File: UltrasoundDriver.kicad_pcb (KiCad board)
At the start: 2 copper layers, 113.8 x 41.1 mm, 52 parts, among them J1 Conn_01x05_Female, J2 Conn_01x05_Female, Q1 S8050, Q2 S8550, U1 MC33079, U2 L7815, U3 L7915, U4 MC33079

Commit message: first board iteration, JLC not done yet. Lotsa DRC errors tho
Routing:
- net Net-(LS1-Pad1): track 34.0 -> 29.0 mm
- net Net-(R16-Pad2): track 50.1 -> 48.7 mm
- net sigIn: track 70.6 -> 69.5 mm
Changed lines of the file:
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@@
   )
   (setup
+    (stackup
+      (layer "F.SilkS" (type "Top Silk Screen"))
+      (layer "F.Paste" (type "Top Solder Paste"))
+      (layer "F.Mask" (type "Top Solder Mask") (thickness 0.01))
+      (layer "F.Cu" (type "copper") (thickness 0.035))
+      (layer "dielectric 1" (type "core") (thickness 1.51) (material "FR4") (epsilon_r 4.5) (loss_tangent 0.02))
+      (layer "B.Cu" (type "copper") (thickness 0.035))
+      (layer "B.Mask" (type "Bottom Solder Mask") (thickness 0.01))
+      (layer "B.Paste" (type "Bottom Solder Paste"))
+      (layer "B.SilkS" (type "Bottom Silk Screen"))
+      (copper_finish "None")
+      (dielectric_constraints no)
+    )
     (pad_to_mask_clearance 0)
     (pcbplotparams
@@
   (segment (start 117.1956 39.9288) (end 124.535923 39.9288) (width 0.25) (layer "B.Cu") (net 1))
   (segment (start 99.0092 40.4368) (end 99.0092 39.9288) (width 0.25) (layer "B.Cu") (net 1))
-  (segment (start 100.2792 39.9288) (end 117.1956 39.9288) (width 0.25) (layer "B.Cu") (net 1))
   (segment (start 98.044 41.402) (end 99.0092 40.4368) (width 0.25) (layer "B.Cu") (net 1))
   (segment (start 69.083 48.26) (end 74.447 53.624) (width 0.25) (layer "B.Cu") (net 1))
   (segment (start 131.831 48.509) (end 103.886 76.454) (width 0.25) (layer "B.Cu") (net 1))
   (segment (start 48.26 48.26) (end 48.26 43.688) (width 0.25) (layer "B.Cu") (net 1))
-  (segment (start 99.0092 39.9288) (end 100.2792 39.9288) (width 0.25) (layer "B.Cu") (net 1))
+  (segment (start 99.0092 39.9288) (end 117.1956 39.9288) (width 0.25) (layer "B.Cu") (net 1))
   (segment (start 74.447 53.624) (end 88.1422 39.9288) (width 0.25) (layer "B.Cu") (net 1))
   (segment (start 94.488 71.244) (end 94.488 73.1898) (width 0.25) (layer "F.Cu") (net 2))
@@
   (segment (start 97.028 44.196) (end 97.028 46.039) (width 0.25) (layer "F.Cu") (net 17))
   (segment (start 97.282 43.18) (end 97.282 43.942) (width 0.25) (layer "F.Cu") (net 17))
-  (segment (start 73.655 57.912) (end 74.447 58.704) (width 0.25) (layer "F.Cu") (net 17))
   (segment (start 97.282 43.942) (end 97.028 44.196) (width 0.25) (layer "F.Cu") (net 17))
   (via (at 97.282 43.18) (size 0.8) (drill 0.4) (layers "F.Cu" "B.Cu") (net 17))
@@
   (segment (start 97.536 38.862) (end 98.298 39.624) (width 0.25) (layer "F.Cu") (net 20))
   (segment (start 80.4164 42.2148) (end 82.487 42.2148) (width 0.25) (layer "F.Cu") (net 20))
-  (segment (start 98.298 46.039) (end 98.298 46.486462) (width 0.25) (layer "F.Cu") (net 20))
   (segment (start 82.487 42.2148) (end 85.8398 38.862) (width 0.25) (layer "F.Cu") (net 20))
   (segment (start 93.218 46.99) (end 93.218 46.039) (width 0.25) (layer "F.Cu") (net 21))
@@
   (segment (start 88.664538 72.81) (end 91.624538 69.85) (width 0.25) (layer "F.Cu") (net 22))
   (segment (start 92.71 69.85) (end 93.218 70.358) (width 0.25) (layer "F.Cu") (net 22))
-  (segment (start 100.3672 58.9652) (end 99.314 57.912) (width 0.25) (layer "F.Cu") (net 23))
+  (segment (start 98.544 57.142) (end 100.3672 58.9652) (width 0.25) (layer "F.Cu") (net 23))
   (segment (start 105.2068 58.1152) (end 104.3568 58.9652) (width 0.25) (layer "F.Cu") (net 23))
-  (segment (start 98.544 57.142) (end 99.441 58.039) (width 0.25) (layer "F.Cu") (net 23))
   (segment (start 98.544 52.824) (end 98.544 57.142) (width 0.25) (layer "F.Cu") (net 23))
   (segment (start 104.3568 58.9652) (end 100.3672 58.9652) (width 0.25) (layer "F.Cu") (net 23))
@@
   (segment (start 103.5568 54.1142) (end 103.569 54.102) (width 0.25) (layer "F.Cu") (net 24))
   (segment (start 99.568 50.989) (end 100.456 50.989) (width 0.25) (layer "F.Cu") (net 24))
-  (segment (start 103.5568 58.0908) (end 103.5568 58.1152) (width 0.25) (layer "F.Cu") (net 24))
-  (segment (start 103.886 54.419) (end 103.569 54.102) (width 0.25) (layer "F.Cu") (net 24))
   (segment (start 100.456 50.989) (end 103.569 54.102) (width 0.25) (layer "F.Cu") (net 24))
   (segment (start 90.936462 48.26) (end 71.374 48.26) (width 0.25) (layer "F.Cu") (net 25))
@@
   (segment (start 88.6318 54.3052) (end 91.948 50.989) (width 0.25) (layer "F.Cu") (net 26))
   (segment (start 64.657 39.681) (end 62.407 39.681) (width 0.25) (layer "F.Cu") (net 26))
-  (segment (start 91.948 50.989) (end 91.948 50.541538) (width 0.25) (layer "F.Cu") (net 26))
   (segment (start 61.468 50.353206) (end 64.039795 52.925001) (width 0.25) (layer "F.Cu") (net 26))
   (segment (start 73.331 52.399) (end 82.2308 52.399) (width 0.25) (layer "F.Cu") (net 26))
-  (segment (start 65.004 39.878) (end 65.707 40.581) (width 0.25) (layer "F.Cu") (net 26))
   (segment (start 65.707 40.581) (end 65.557 40.581) (width 0.25) (layer "F.Cu") (net 26))
   (segment (start 62.407 39.681) (end 61.468 40.62) (width 0.25) (layer "F.Cu") (net 26))
@@
   (segment (start 124.142 42.7096) (end 125.5136 42.7096) (width 0.25) (layer "F.Cu") (net 28))
   (segment (start 124.142 40.0812) (end 124.142 42.7096) (width 0.25) (layer "F.Cu") (net 28))
-  (segment (start 130.556 47.752) (end 127.03 44.226) (width 0.25) (layer "B.Cu") (net 28))
   (zone (net 2) (net_name "GND") (layers F&B.Cu) (hatch edge 0.508)
     (connect_pads (clearance 0.508))

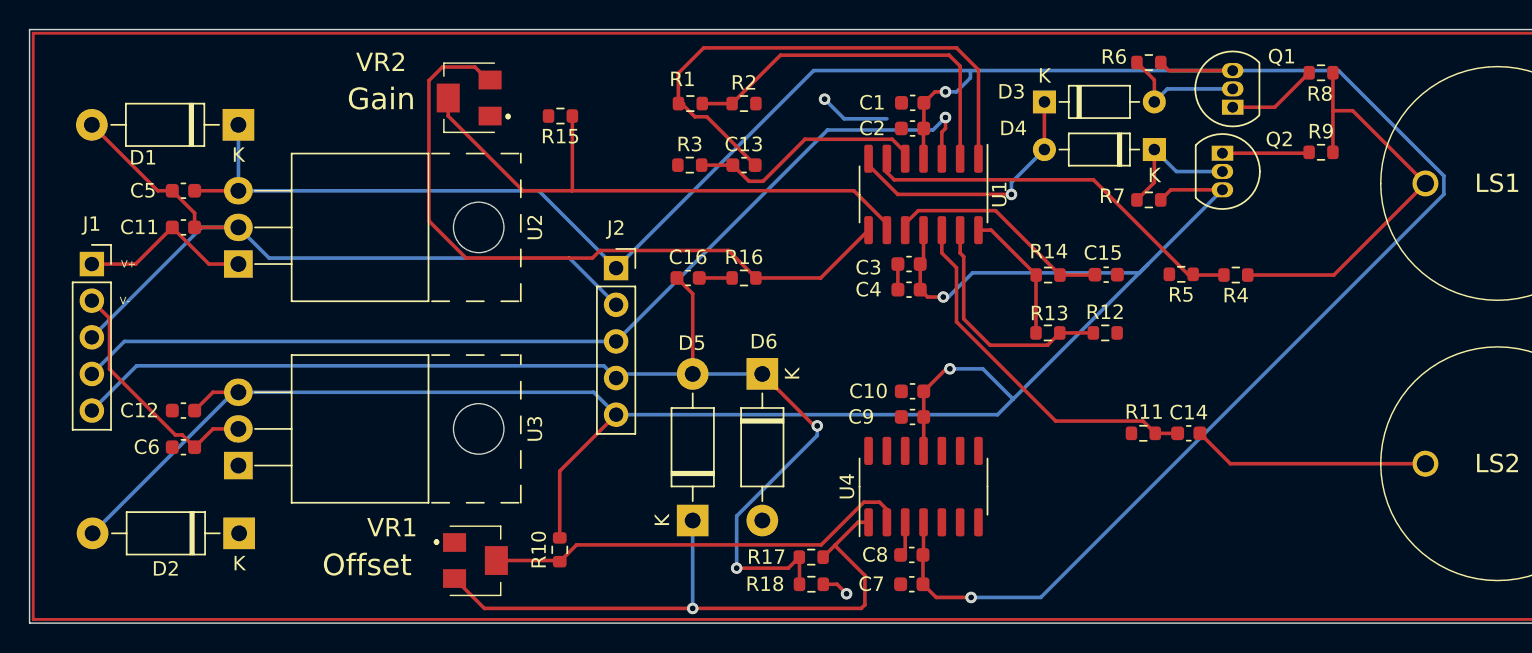
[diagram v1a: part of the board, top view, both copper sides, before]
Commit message: yeah I think this one is better, also updated resistor values after lab work
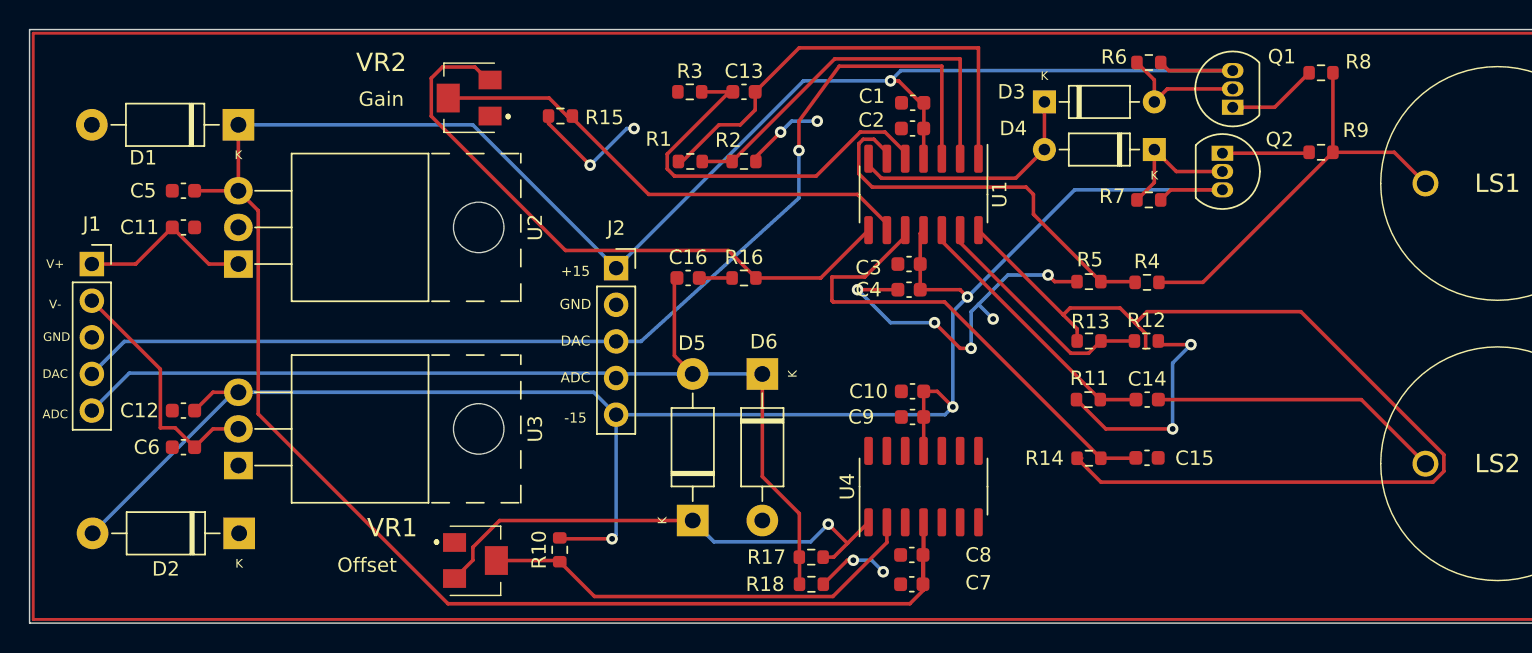
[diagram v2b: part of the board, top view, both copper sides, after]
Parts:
- R15: value 10k -> 100
- R4: value 4.7k -> 5.8k
- moved R14 13.0 mm to (107.2, 66.8)
- moved C15 13.0 mm to (111.3, 66.8)
- moved R5 6.42 mm to (107.2, 54.6)
- moved R4 6.18 mm to (111.3, 54.6)
- moved C13 5.08 mm to (83.3, 41.4)
- moved R3 5.08 mm to (79.6, 41.4)
- moved R11 4.47 mm to (107.2, 62.7)
- moved R1 4.01 mm to (79.6, 46.2)
- moved R2 4.01 mm to (83.3, 46.2)
- moved C14 3.71 mm to (111.3, 62.7)
- moved R12 2.91 mm to (111.2, 58.7)
- moved R13 2.91 mm to (107.2, 58.7)
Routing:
- net Net-(R13-Pad2): track 9.31 -> 71.9 mm
- net Net-(C15-Pad2): track 15.8 -> 33.9 mm
- net -15V: track 140.7 -> 128.2 mm, vias 2 -> 3
- net Net-(C13-Pad1): track 16.6 -> 28.5 mm
- net 3.3V: track 44.6 -> 35.3 mm
- net sigOut: track 79.4 -> 70.7 mm, vias 2 -> 0
- net sigIn: track 69.5 -> 77.4 mm
- net Net-(C14-Pad1): track 25.3 -> 18.8 mm
- net +15V: track 169.3 -> 175.4 mm, vias 2 -> 1
- net Net-(R15-Pad1): track 40.4 -> 34.5 mm
- net GND: track 66.5 -> 60.6 mm, vias 2 -> 13
- net Net-(C13-Pad2): track 37.9 -> 32.5 mm
- net Net-(R16-Pad2): track 48.7 -> 43.7 mm
- net Net-(C14-Pad2): track 16.5 -> 20.4 mm
- net Net-(R1-Pad2): track 26.0 -> 27.8 mm
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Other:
- board text added: "+15"
- board text added: "-15"
- board text added: "ADC"
- board text added: "DAC"
- board text added: "GND"

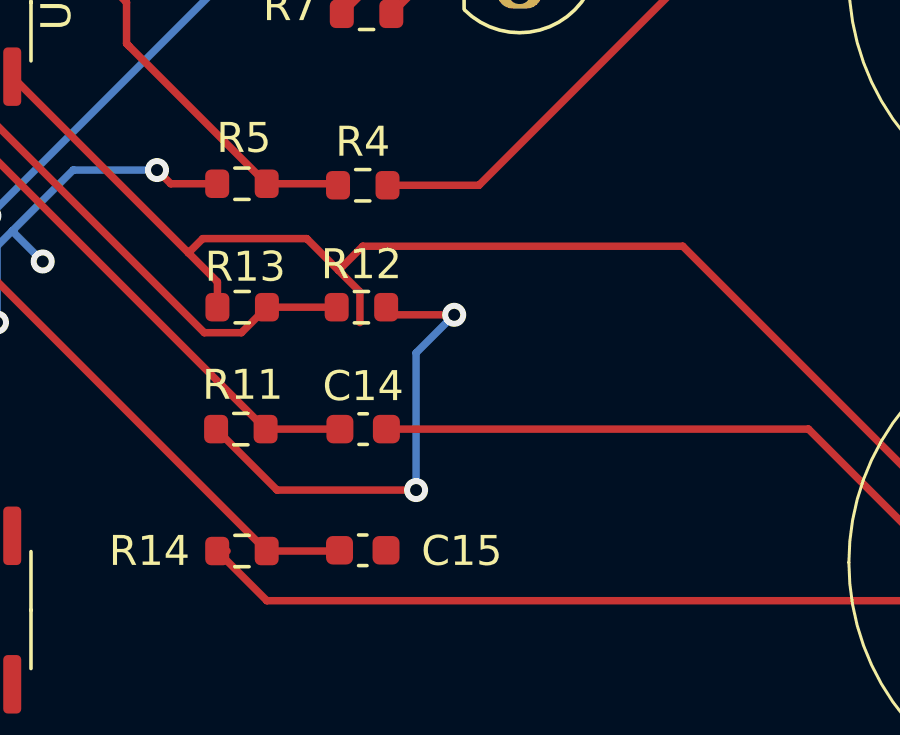
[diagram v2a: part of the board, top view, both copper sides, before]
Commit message: need to change footprint for tantalum caps
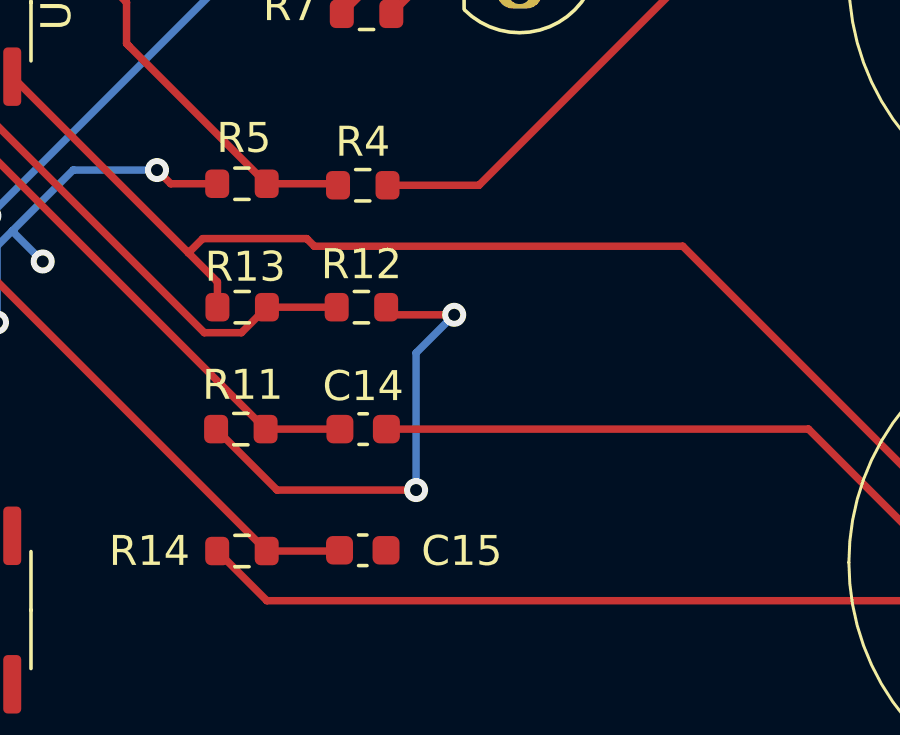
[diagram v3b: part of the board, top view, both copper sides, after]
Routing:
- net Net-(R13-Pad2): track 71.9 -> 68.9 mm
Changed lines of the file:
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@@
   (segment (start 103.4532 49.9628) (end 108.0496 54.5592) (width 0.25) (layer "F.Cu") (net 21))
   (segment (start 108.0496 54.5592) (end 110.3762 54.5592) (width 0.25) (layer "F.Cu") (net 21))
-  (segment (start 108.1004 54.61) (end 108.0496 54.5592) (width 0.25) (layer "F.Cu") (net 21))
   (segment (start 92.315462 44.689) (end 91.580538 44.689) (width 0.25) (layer "F.Cu") (net 21))
   (segment (start 93.218 45.591538) (end 92.315462 44.689) (width 0.25) (layer "F.Cu") (net 21))
@@
   (segment (start 108.0577 58.674) (end 107.2077 59.524) (width 0.25) (layer "F.Cu") (net 23))
   (segment (start 105.969527 59.524) (end 98.298 51.852473) (width 0.25) (layer "F.Cu") (net 23))
-  (segment (start 131.084123 68.458) (end 131.831 67.711123) (width 0.25) (layer "F.Cu") (net 24))
-  (segment (start 111.1573 59.187173) (end 111.1573 58.160827) (width 0.25) (layer "F.Cu") (net 24))
+  (segment (start 121.92 56.642) (end 109.638473 56.642) (width 0.25) (layer "F.Cu") (net 24))
+  (segment (start 131.831 66.553) (end 121.92 56.642) (width 0.25) (layer "F.Cu") (net 24))
   (segment (start 106.4077 57.8287) (end 105.4425 56.8635) (width 0.25) (layer "F.Cu") (net 24))
-  (segment (start 108.056 68.458) (end 131.084123 68.458) (width 0.25) (layer "F.Cu") (net 24))
-  (segment (start 131.831 66.553) (end 121.92 56.642) (width 0.25) (layer "F.Cu") (net 24))
   (segment (start 106.4 66.802) (end 108.056 68.458) (width 0.25) (layer "F.Cu") (net 24))
   (segment (start 105.4425 56.8635) (end 99.568 50.989) (width 0.25) (layer "F.Cu") (net 24))
+  (segment (start 108.056 68.458) (end 131.084123 68.458) (width 0.25) (layer "F.Cu") (net 24))
+  (segment (start 109.384473 56.388) (end 105.918 56.388) (width 0.25) (layer "F.Cu") (net 24))
+  (segment (start 131.084123 68.458) (end 131.831 67.711123) (width 0.25) (layer "F.Cu") (net 24))
+  (segment (start 109.638473 56.642) (end 109.384473 56.388) (width 0.25) (layer "F.Cu") (net 24))
+  (segment (start 106.4077 58.674) (end 106.4077 57.8287) (width 0.25) (layer "F.Cu") (net 24))
+  (segment (start 105.918 56.388) (end 105.4425 56.8635) (width 0.25) (layer "F.Cu") (net 24))
   (segment (start 131.831 67.711123) (end 131.831 66.553) (width 0.25) (layer "F.Cu") (net 24))
-  (segment (start 111.1573 58.160827) (end 110.445236 57.448764) (width 0.25) (layer "F.Cu") (net 24))
-  (segment (start 111.252 56.642) (end 110.445236 57.448764) (width 0.25) (layer "F.Cu") (net 24))
-  (segment (start 106.4 66.802) (end 106.729073 66.802) (width 0.25) (layer "F.Cu") (net 24))
-  (segment (start 105.918 56.388) (end 105.4425 56.8635) (width 0.25) (layer "F.Cu") (net 24))
-  (segment (start 110.445236 57.448764) (end 109.384473 56.388) (width 0.25) (layer "F.Cu") (net 24))
-  (segment (start 106.4077 58.674) (end 106.4077 57.8287) (width 0.25) (layer "F.Cu") (net 24))
-  (segment (start 121.92 56.642) (end 111.252 56.642) (width 0.25) (layer "F.Cu") (net 24))
-  (segment (start 109.384473 56.388) (end 105.918 56.388) (width 0.25) (layer "F.Cu") (net 24))
   (segment (start 93.218 50.541538) (end 91.190462 48.514) (width 0.25) (layer "F.Cu") (net 25))
   (segment (start 69.802373 41.831) (end 71.049773 43.0784) (width 0.25) (layer "F.Cu") (net 25))

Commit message: this draft has gone to justin
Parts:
- C11, C12, C5, C6: footprint Capacitor_SMD:C_0603_1608Metric -> Capacitor_Tantalum_SMD:CP_EIA-3216-18_Kemet-A
- D1, D2: value 1N4001 -> 1N4148W; footprint Diode_THT:D_DO-41_SOD81_P10.16mm_Horizontal -> Diode_SMD:D_SOD-123
- D3, D4: value 1N914 -> 1N4148W; footprint Diode_THT:D_DO-35_SOD27_P7.62mm_Horizontal -> Diode_SMD:D_SOD-123
- D5, D6: value 1N5819 -> B5819W.SL; footprint Diode_THT:D_DO-41_SOD81_P10.16mm_Horizontal -> SamacSys_Parts:B5819WSL
- Q1: value S8050 -> SS8050-G; footprint Package_TO_SOT_THT:TO-92_Inline -> SamacSys_Parts:SOT95P240X115-3N
- Q2: footprint Package_TO_SOT_THT:TO-92_Inline -> SamacSys_Parts:SOT95P240X115-3N
- R4: value 5.8k -> 6.8k
- moved D6 5.93 mm to (85.6, 66.8), turned to 90 degrees
- moved D2 5.13 mm to (43.2, 72.1)
- moved D1 5.08 mm to (43.2, 43.7)
- moved D4 4.95 mm to (106.8, 45.5)
- moved D5 4.32 mm to (79.8, 66.8)
- moved Q1 3.39 mm to (119.4, 39.9)
- moved D3 2.67 mm to (106.8, 42.2)
- moved Q2 2.53 mm to (118.9, 46.5), turned to 90 degrees
- moved C5 1.62 mm to (42.8, 51.1)
- moved C11 1.52 mm to (42.9, 48.3)
- moved C12 1.44 mm to (43.4, 62.5)
- moved C6 1.33 mm to (43.4, 65.3)
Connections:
- D3 pad 2: Net-(D3-Pad2) -> Net-(R6-Pad2)
- D4 pad 1: Net-(D4-Pad1) -> Net-(R7-Pad1)
- Q1 pad 1: Net-(Q1-Pad1) -> Net-(R6-Pad2)
- Q1 pad 2: Net-(D3-Pad2) -> Net-(R8-Pad1)
- Q2 pad 1: Net-(Q2-Pad1) -> Net-(R7-Pad1)
- Q2 pad 2: Net-(D4-Pad1) -> Net-(R9-Pad1)
- R6 pad 2: Net-(D3-Pad2) -> Net-(R6-Pad2)
- R7 pad 1: Net-(D4-Pad1) -> Net-(R7-Pad1)
- R8 pad 1: Net-(Q1-Pad1) -> Net-(R8-Pad1)
- R9 pad 1: Net-(Q2-Pad1) -> Net-(R9-Pad1)
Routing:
- net Net-(R7-Pad1): track 0.00 -> 12.2 mm
- net Net-(R6-Pad2): track 0.00 -> 12.2 mm
- net -15V: track 128.2 -> 139.2 mm, vias 3 -> 6
- net +15V: track 175.4 -> 185.7 mm, vias 1 -> 3
- net Net-(D4-Pad1): track 9.34 -> 0.00 mm
- net Net-(D3-Pad2): track 9.04 -> 0.00 mm
- net Net-(Q1-Pad1): track 6.29 -> 0.00 mm
- net Net-(Q2-Pad1): track 6.04 -> 0.00 mm
- net sigOut: track 70.7 -> 74.9 mm
- net Net-(R9-Pad1): track 0.00 -> 3.49 mm
- net GND: track 60.6 -> 63.4 mm, vias 13 -> 14
- net 3.3V: track 35.3 -> 38.0 mm, vias 1 -> 2
- net Net-(R8-Pad1): track 0.00 -> 2.53 mm
- net Net-(U1-Pad7): track 17.1 -> 18.1 mm

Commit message: receiver is moved to other side, I am considereding reording the op amp units to not make signal lines too long - almost certainly unnecessary since it breadboarded fine. But still
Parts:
- moved LS1 90.8 mm to (218.3, 71.4)
- moved C12 88.1 mm to (130.6, 75.7)
- moved C3 88.1 mm to (181.9, 66.5)
- moved C4 88.1 mm to (181.9, 68.3)
- moved C7 88.1 mm to (182.1, 88.7)
- moved C8 88.1 mm to (182.1, 86.7)
- moved Q1 88.1 mm to (206.5, 53.1)
- moved R1 88.1 mm to (166.7, 59.4)
- moved R13 88.1 mm to (194.4, 71.9)
- moved R14 88.1 mm to (194.3, 80.0)
- moved R17 88.1 mm to (175.1, 86.9)
- moved U2 88.1 mm to (135.4, 66.5)
- moved U3 88.1 mm to (135.4, 80.5)
- moved VR1 88.1 mm to (151.8, 87.1)
- moved C1 88.1 mm to (182.1, 55.4)
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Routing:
- net Net-(C14-Pad2): track 20.4 -> 106.5 mm
- net Net-(R13-Pad2): track 68.9 -> 17.4 mm
- net Net-(LS1-Pad1): track 28.6 -> 36.8 mm
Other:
- board size 113.8 x 41.1 mm -> 137.3 x 46.2 mm

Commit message: updated and sent to Justin
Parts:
- moved C14 71.9 mm to (126.5, 74.4), turned to 90 degrees
- moved R12 68.1 mm to (130.6, 78.2), turned to -90 degrees
- moved R11 67.9 mm to (126.5, 78.2), turned to -90 degrees
- moved C7 65.0 mm to (123.3, 60.9), turned to 90 degrees
- moved C15 64.0 mm to (134.4, 78.2), turned to 90 degrees
- moved R13 63.8 mm to (130.6, 74.4), turned to 90 degrees
- moved R18 62.4 mm to (123.3, 53.9), turned to 90 degrees
- moved C8 62.3 mm to (125.4, 60.9), turned to 90 degrees
- moved R14 60.2 mm to (134.4, 74.4), turned to -90 degrees
- moved R17 59.8 mm to (125.2, 53.9), turned to -90 degrees
- moved U4 56.5 mm to (130.1, 61.7), turned to 0 degrees
- moved C9 49.9 mm to (134.9, 61.0), turned to 90 degrees
- moved D6 49.6 mm to (132.1, 51.6), turned to 0 degrees
- moved D5 48.9 mm to (132.1, 45.7), turned to 0 degrees
- moved C10 47.6 mm to (136.7, 61.0), turned to 90 degrees
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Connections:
- D3 pad 1: Net-(U1-Pad7) -> Net-(D3-Pad1)
- D4 pad 2: Net-(U1-Pad7) -> Net-(D3-Pad1)
- U1 pad 10: Net-(C15-Pad2) -> (no net)
- U1 pad 12: Net-(C14-Pad1) -> Net-(C13-Pad1)
- U1 pad 13: Net-(R12-Pad1) -> Net-(R4-Pad2)
- U1 pad 14: Net-(R13-Pad2) -> Net-(D3-Pad1)
- U1 pad 5: Net-(C13-Pad1) -> (no net)
- U1 pad 6: Net-(R4-Pad2) -> (no net)
- U1 pad 7: Net-(U1-Pad7) -> (no net)
- U1 pad 8: Net-(R16-Pad2) -> (no net)
- U1 pad 9: Net-(R15-Pad1) -> (no net)
- U4 pad 10: (no net) -> Net-(C15-Pad2)
- U4 pad 5: (no net) -> Net-(C14-Pad1)
- U4 pad 6: (no net) -> Net-(R12-Pad1)
- U4 pad 7: (no net) -> Net-(R13-Pad2)
- U4 pad 8: (no net) -> Net-(R16-Pad2)
- U4 pad 9: (no net) -> Net-(R15-Pad1)
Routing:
- net Net-(C14-Pad2): track 106.5 -> 16.5 mm
- net sigOut: track 74.9 -> 149.9 mm
- net Net-(R10-Pad1): track 31.1 -> 74.8 mm, vias 0 -> 2
- net -15V: track 139.2 -> 180.0 mm, vias 6 -> 2
- net Net-(R16-Pad2): track 43.7 -> 83.8 mm
- net 3.3V: track 38.0 -> 77.0 mm, vias 2 -> 3
- net Net-(R15-Pad1): track 34.5 -> 72.1 mm
- net sigIn: track 77.4 -> 55.5 mm, vias 1 -> 0
- net Net-(D3-Pad1): track 0.00 -> 19.9 mm
- net GND: track 63.4 -> 45.2 mm, vias 14 -> 4
- net Net-(U1-Pad7): track 18.1 -> 0.00 mm
- net +15V: track 185.7 -> 167.8 mm
- net Net-(C15-Pad2): track 33.9 -> 18.6 mm
- net Net-(R4-Pad2): track 28.1 -> 13.5 mm
- net Net-(R1-Pad2): track 27.8 -> 16.5 mm
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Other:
- board text added: "test"
